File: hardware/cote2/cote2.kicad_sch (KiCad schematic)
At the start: 5 parts, among them J1 USB-307HB-B-SU, J2 Vers J14 Main, U1 USBLC6-2SC6

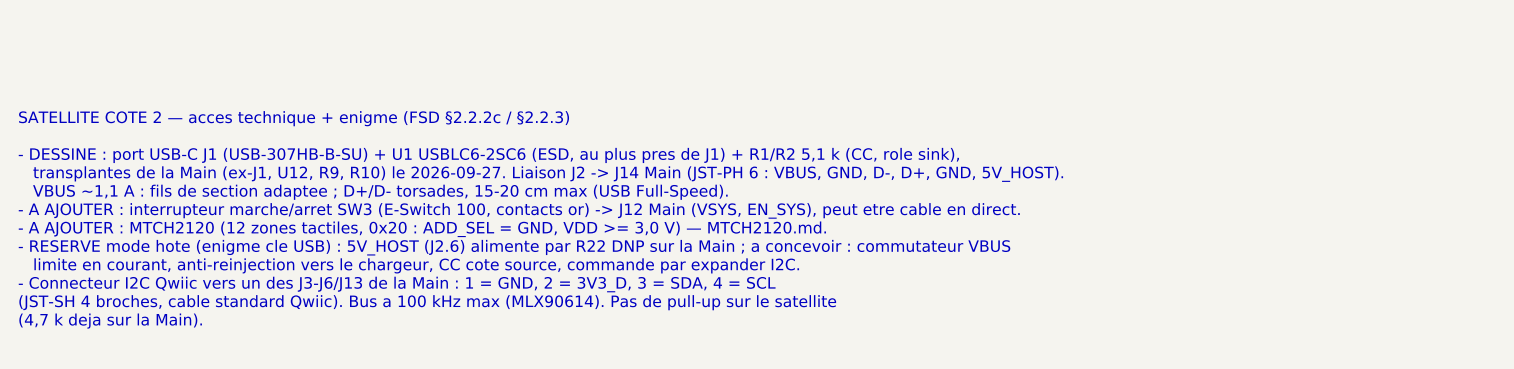
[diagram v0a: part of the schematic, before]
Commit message: hardware+docs: CAP1298 retenu pour le tactile de Cote 2, BOM de reference corrigee (H8)
- Cote 2 : CAP1298-1-SL-TR (C2652072, 8 touches, 0x28 fixe) remplace le MTCH2120
  (aucun stock) ; proximite de Cote 3 en suspens (pas de second CAP12xx).
- BOM : U11 = LSM6DSOXTR, doublon U21 retire, filtre DAC 470 ohm + 2,2 nF C0G,
  TMAG5273A1 (C3716049), U10 SOT-23-6, ecran bouche a choisir, LCSC de D1/Q1/Q2
  dans la bonne colonne, ST25DV et haut-parleur ajoutes.
- docs/pcb/02-bom-lcsc.csv (perimee) supprimee : une seule BOM.
- FSD, RESTE-A-FAIRE, syntheses et cartouches satellites alignes.
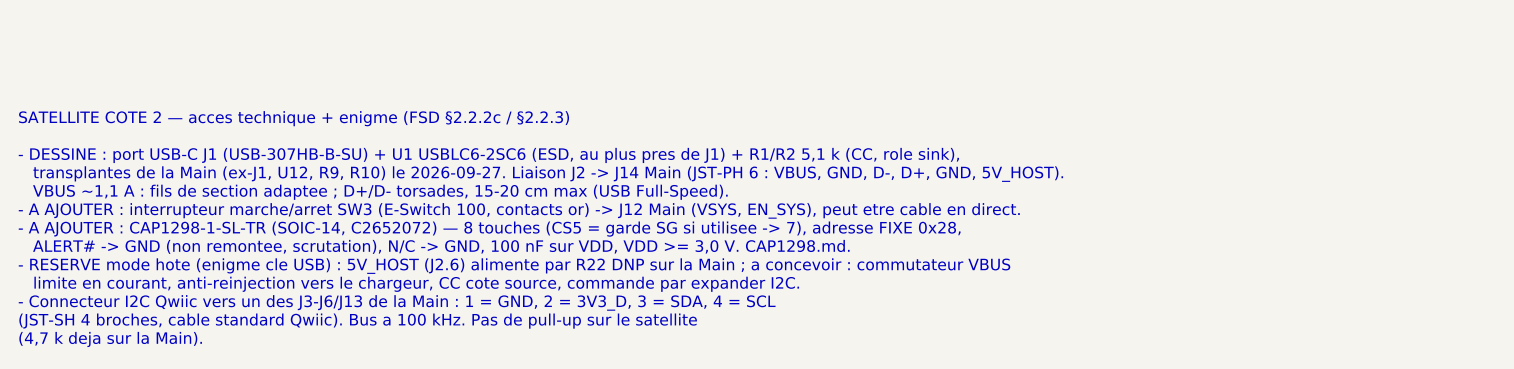
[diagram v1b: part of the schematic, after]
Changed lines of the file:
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@@
 		)
 	)
-	(text "SATELLITE COTE 2 — acces technique + enigme (FSD §2.2.2c / §2.2.3)\n\n- DESSINE : port USB-C J1 (USB-307HB-B-SU) + U1 USBLC6-2SC6 (ESD, au plus pres de J1) + R1/R2 5,1 k (CC, role sink),\n   transplantes de la Main (ex-J1, U12, R9, R10) le 2026-09-27. Liaison J2 -> J14 Main (JST-PH 6 : VBUS, GND, D-, D+, GND, 5V_HOST).\n   VBUS ~1,1 A : fils de section adaptee ; D+/D- torsades, 15-20 cm max (USB Full-Speed).\n- A AJOUTER : interrupteur marche/arret SW3 (E-Switch 100, contacts or) -> J12 Main (VSYS, EN_SYS), peut etre cable en direct.\n- A AJOUTER : MTCH2120 (12 zones tactiles, 0x20 : ADD_SEL = GND, VDD >= 3,0 V) — MTCH2120.md.\n- RESERVE mode hote (enigme cle USB) : 5V_HOST (J2.6) alimente par R22 DNP sur la Main ; a concevoir : commutateur VBUS\n   limite en courant, anti-reinjection vers le chargeur, CC cote source, commande par expander I2C.\n- Connecteur I2C Qwiic vers un des J3-J6/J13 de la Main : 1 = GND, 2 = 3V3_D, 3 = SDA, 4 = SCL\n(JST-SH 4 broches, cable standard Qwiic). Bus a 100 kHz max (MLX90614). Pas de pull-up sur le satellite\n(4,7 k deja sur la Main)."
+	(text "SATELLITE COTE 2 — acces technique + enigme (FSD §2.2.2c / §2.2.3)\n\n- DESSINE : port USB-C J1 (USB-307HB-B-SU) + U1 USBLC6-2SC6 (ESD, au plus pres de J1) + R1/R2 5,1 k (CC, role sink),\n   transplantes de la Main (ex-J1, U12, R9, R10) le 2026-09-27. Liaison J2 -> J14 Main (JST-PH 6 : VBUS, GND, D-, D+, GND, 5V_HOST).\n   VBUS ~1,1 A : fils de section adaptee ; D+/D- torsades, 15-20 cm max (USB Full-Speed).\n- A AJOUTER : interrupteur marche/arret SW3 (E-Switch 100, contacts or) -> J12 Main (VSYS, EN_SYS), peut etre cable en direct.\n- A AJOUTER : CAP1298-1-SL-TR (SOIC-14, C2652072) — 8 touches (CS5 = garde SG si utilisee -> 7), adresse FIXE 0x28,\n   ALERT# -> GND (non remontee, scrutation), N/C -> GND, 100 nF sur VDD, VDD >= 3,0 V. CAP1298.md.\n- RESERVE mode hote (enigme cle USB) : 5V_HOST (J2.6) alimente par R22 DNP sur la Main ; a concevoir : commutateur VBUS\n   limite en courant, anti-reinjection vers le chargeur, CC cote source, commande par expander I2C.\n- Connecteur I2C Qwiic vers un des J3-J6/J13 de la Main : 1 = GND, 2 = 3V3_D, 3 = SDA, 4 = SCL\n(JST-SH 4 broches, cable standard Qwiic). Bus a 100 kHz. Pas de pull-up sur le satellite\n(4,7 k deja sur la Main)."
 		(exclude_from_sim no)
 		(at 20.32 142.24 0)

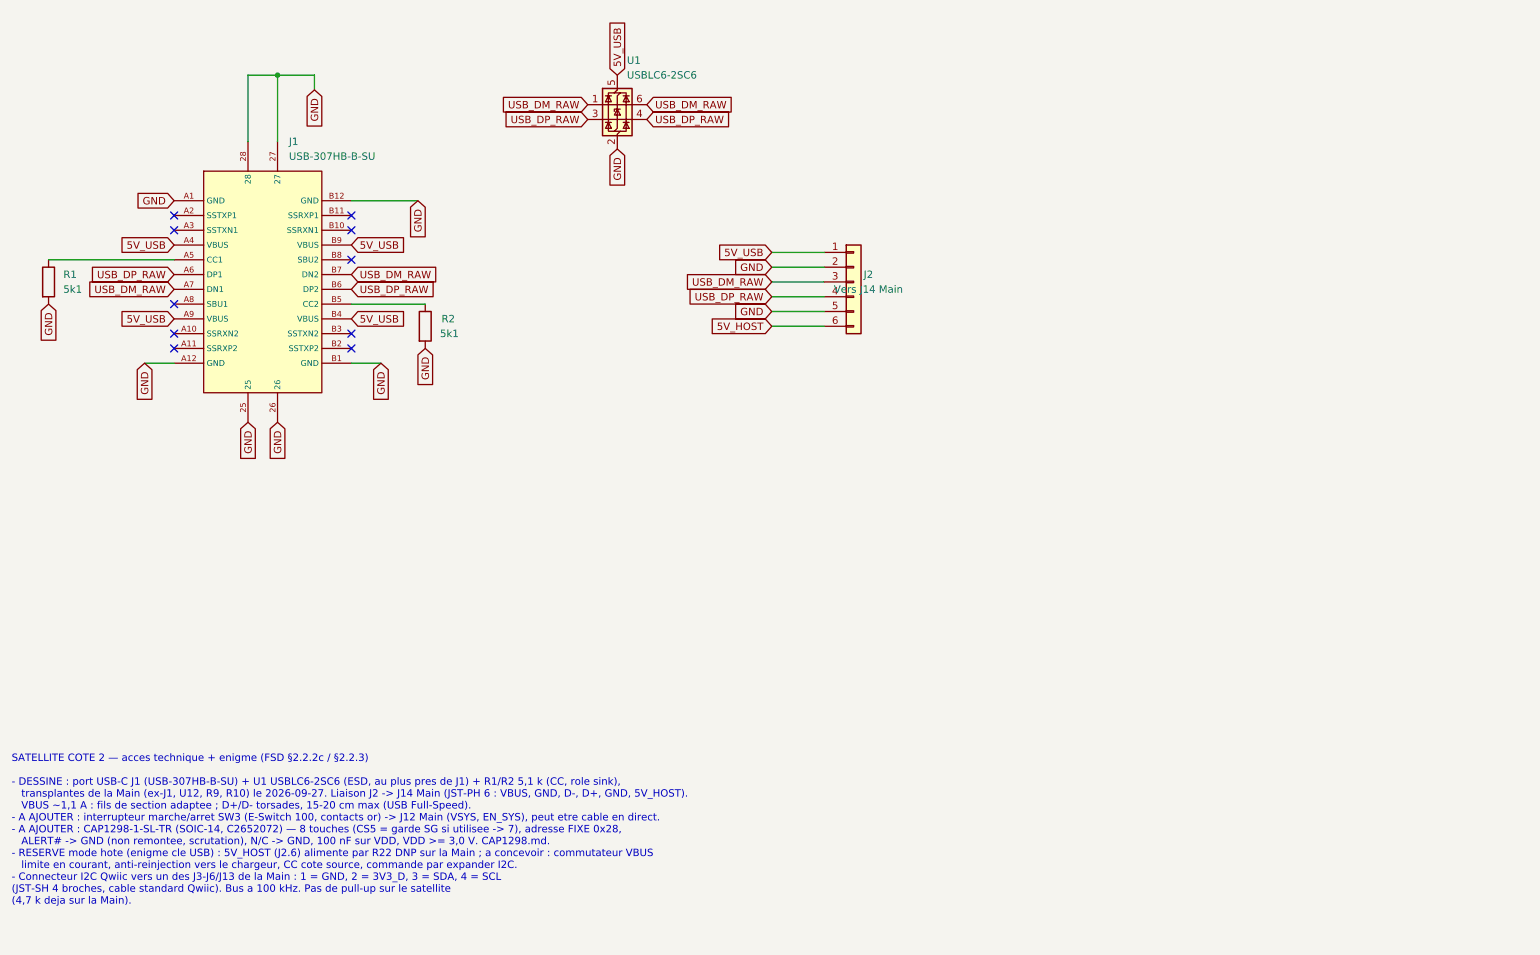
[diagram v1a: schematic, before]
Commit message: hardware(cote2): partie tactile CAP1298 dessinee, approche ta main sur Cote 2
- U2 CAP1298 (0x28), C1 100 nF + C2 1 uF (figure 3-1), J3 Qwiic, ALERT# et N/C a GND.
- 6 touches (CS1-4, CS6, CS7), proximite CS8 gardee par SG (CS5), electrodes
  E1-E8 sur le PCB (TestPoint provisoires, hors BOM). Netlist verifiee.
- Cote 3 = TMAG5273 seul. Bibliotheque : CAP1298 importe, MLX90614 et
  MTCH2120 retires. BOM, FSD, RESTE-A-FAIRE et synthese CAP1298 alignes.
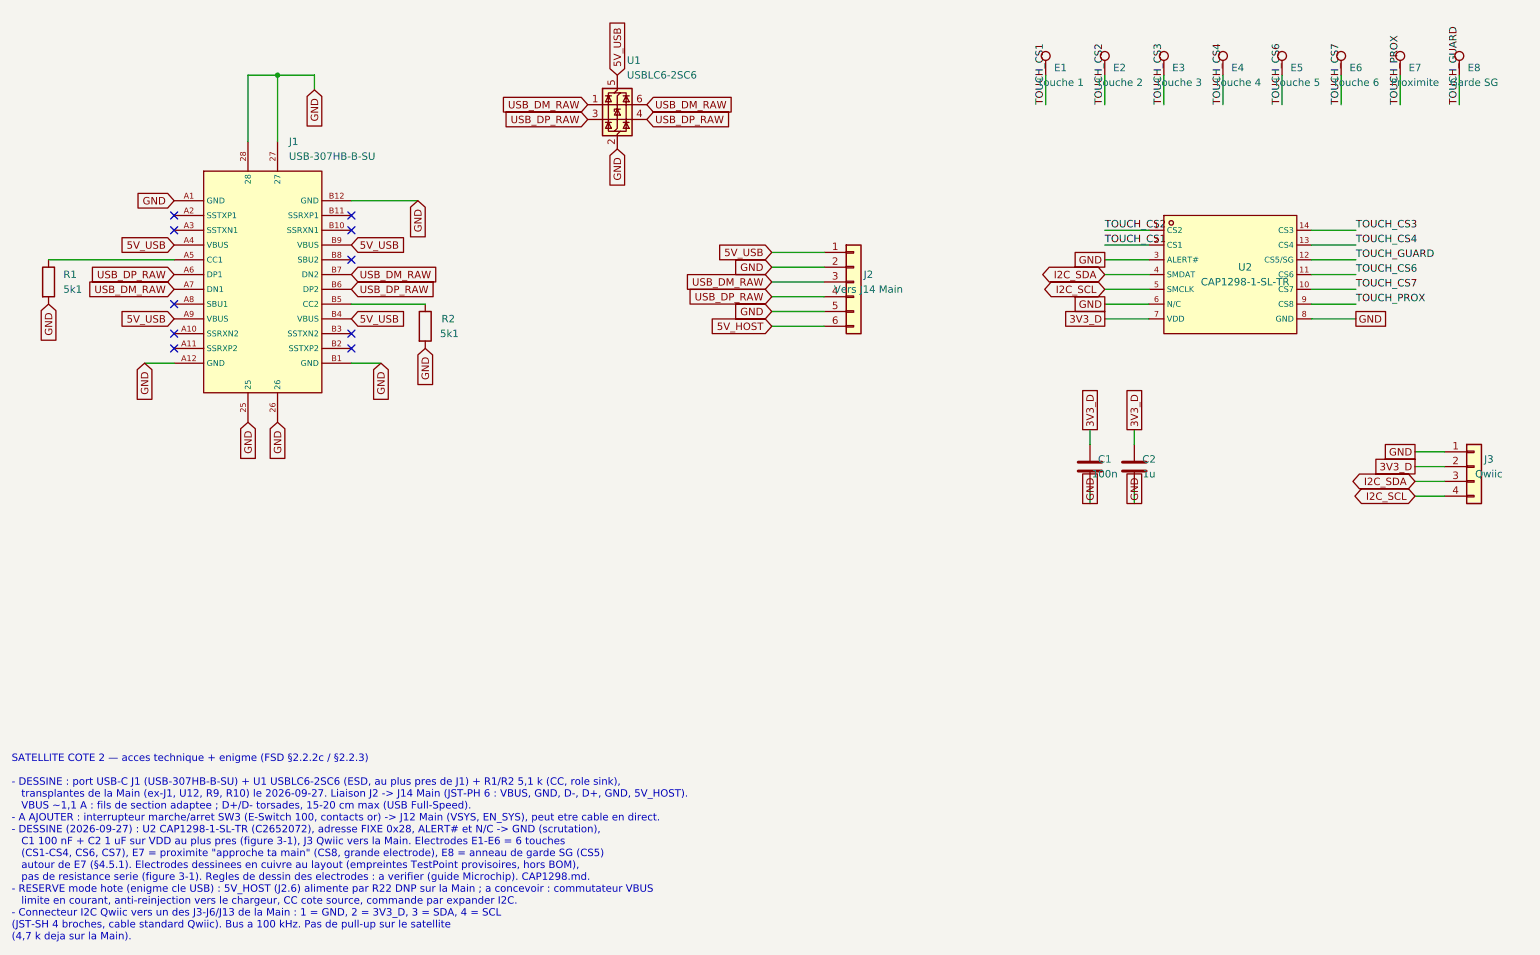
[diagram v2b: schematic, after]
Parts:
- added C1: 100n, Capacitor_SMD:C_0402_1005Metric, symbol Device:C
- added C2: 1u, Capacitor_SMD:C_0402_1005Metric, symbol Device:C
- added E1: Touche 1, TestPoint:TestPoint_Pad_D4.0mm, symbol Connector:TestPoint
- added E2: Touche 2, TestPoint:TestPoint_Pad_D4.0mm, symbol Connector:TestPoint
- added E3: Touche 3, TestPoint:TestPoint_Pad_D4.0mm, symbol Connector:TestPoint
- added E4: Touche 4, TestPoint:TestPoint_Pad_D4.0mm, symbol Connector:TestPoint
- added E5: Touche 5, TestPoint:TestPoint_Pad_D4.0mm, symbol Connector:TestPoint
- added E6: Touche 6, TestPoint:TestPoint_Pad_D4.0mm, symbol Connector:TestPoint
- added E7: Proximite, TestPoint:TestPoint_Pad_D4.0mm, symbol Connector:TestPoint
- added E8: Garde SG, TestPoint:TestPoint_Pad_D4.0mm, symbol Connector:TestPoint
- added J3: Qwiic, Connector_JST:JST_SH_BM04B-SRSS-TB_1x04-1MP_P1.00mm_Vertical, symbol Connector_Generic:Conn_01x04
- added U2: CAP1298-1-SL-TR, lcsc_footprints:C2652072_SOIC-14_L8_7-W3_9-P1_27-LS6_0-BL, symbol lcsc_imported:CAP1298-1-SL-TR
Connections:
- net GND: now also C1.2, C2.2, J3.1 (Pin_1), U2.3 (ALERT#), U2.6 (N/C), U2.8 (GND)
- new net 3V3_D: C1.1, C2.1, J3.2 (Pin_2), U2.7 (VDD)
- new net I2C_SCL: J3.4 (Pin_4), U2.5 (SMCLK)
- new net I2C_SDA: J3.3 (Pin_3), U2.4 (SMDAT)
- new net TOUCH_CS1: E1.1, U2.2 (CS1)
- new net TOUCH_CS2: E2.1, U2.1 (CS2)
- new net TOUCH_CS3: E3.1, U2.14 (CS3)
- new net TOUCH_CS4: E4.1, U2.13 (CS4)
- new net TOUCH_CS6: E5.1, U2.11 (CS6)
- new net TOUCH_CS7: E6.1, U2.10 (CS7)
- new net TOUCH_GUARD: E8.1, U2.12 (CS5/SG)
- new net TOUCH_PROX: E7.1, U2.9 (CS8)

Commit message: main: pastilles UART0 TP_TXD0/TP_RXD0 ; SW3 cable en direct sur J12 (modele a rechoisir)
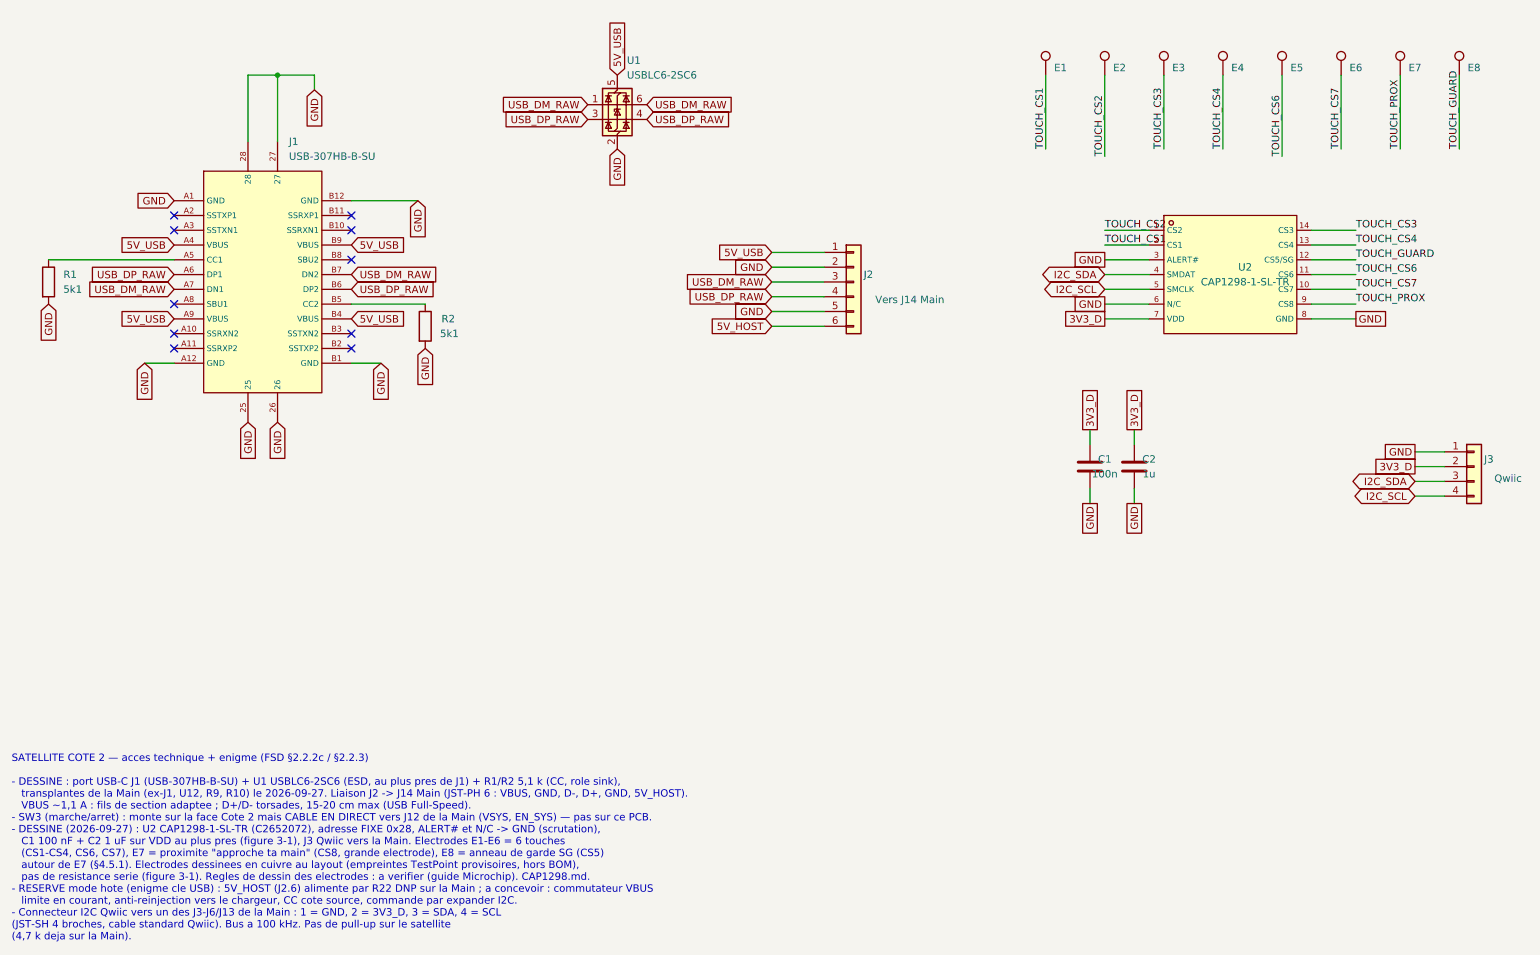
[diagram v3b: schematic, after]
